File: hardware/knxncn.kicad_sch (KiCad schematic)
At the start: 23 parts, among them U1 NCN5130, X1 FA-238

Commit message: Switch to STM32U575CIT6
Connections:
- net GND: now also U1.23 (MODE1), U1.24 (MODE2), U1.25 (TREQ), U1.26 (CSB/UC1), U1.29 (SCK/UC2)
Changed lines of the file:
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@@
   (junction (at 186.69 85.09) (diameter 0) (color 0 0 0 0)
   )
+  (junction (at 179.07 72.39) (diameter 0) (color 0 0 0 0)
+  )
   (junction (at 96.52 77.47) (diameter 0) (color 0 0 0 0)
   )
@@
   )
   (junction (at 124.46 110.49) (diameter 0) (color 0 0 0 0)
+  )
+  (junction (at 179.07 69.85) (diameter 0) (color 0 0 0 0)
   )
   (junction (at 161.29 110.49) (diameter 0) (color 0 0 0 0)
@@
     (stroke (width 0) (type default) (color 0 0 0 0))
   )
+  (wire (pts (xy 179.07 69.85) (xy 179.07 72.39))
+    (stroke (width 0) (type default) (color 0 0 0 0))
+  )
   (wire (pts (xy 105.41 87.63) (xy 105.41 85.09))
     (stroke (width 0) (type default) (color 0 0 0 0))
@@
     (stroke (width 0) (type default) (color 0 0 0 0))
   )
-  (wire (pts (xy 165.1 72.39) (xy 186.69 72.39))
+  (wire (pts (xy 165.1 72.39) (xy 179.07 72.39))
     (stroke (width 0) (type default) (color 0 0 0 0))
   )
@@
     (stroke (width 0) (type default) (color 0 0 0 0))
   )
+  (wire (pts (xy 179.07 72.39) (xy 186.69 72.39))
+    (stroke (width 0) (type default) (color 0 0 0 0))
+  )

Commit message: Progress
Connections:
- net GND is gone; now on net GNDREF: C6.2, U1.23 (MODE1), U1.24 (MODE2), U1.25 (TREQ), U1.26 (CSB/UC1), U1.29 (SCK/UC2), U1.31 (VSSD), U1.33 (XSEL), U1.41 (GND)
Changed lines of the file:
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@@
   (junction (at 77.47 92.71) (diameter 0) (color 0 0 0 0)
+  )
+  (junction (at 186.69 87.63) (diameter 0) (color 0 0 0 0)
   )
   (junction (at 168.91 69.85) (diameter 0) (color 0 0 0 0)
@@
     (effects (font (size 1.27 1.27)) (justify left bottom))
   )
-  (label "KNX-" (at 77.47 102.87 180)
-    (effects (font (size 1.27 1.27)) (justify right bottom))
-  )
-  (hierarchical_label "KNX_GND" (shape output) (at 176.53 133.35 0)
+  (hierarchical_label "GNDREF" (shape output) (at 176.53 133.35 0)
     (effects (font (size 1.27 1.27)) (justify left))
   )
@@
     (effects (font (size 1.27 1.27)) (justify right))
   )
-  (hierarchical_label "KNX_V12" (shape output) (at 111.76 106.68 180)
+  (hierarchical_label "+12V" (shape output) (at 111.76 106.68 180)
     (effects (font (size 1.27 1.27)) (justify right))
   )
@@
     (effects (font (size 1.27 1.27)) (justify left))
   )
-  (hierarchical_label "KNX_V3.3" (shape output) (at 173.99 104.14 0)
+  (hierarchical_label "+3.3V" (shape output) (at 173.99 104.14 0)
     (effects (font (size 1.27 1.27)) (justify left))
   )
@@
     (pin "2")
   )
-  (symbol (lib_id "power:GND") (at 153.67 52.07 180) (unit 1)
-    (in_bom yes) (on_board yes)
-    (property "Reference" "#PWR0130" (id 0) (at 153.67 45.72 0)
-      (effects (font (size 1.27 1.27)) hide)
-    )
-    (property "Value" "GND" (id 1) (at 153.543 47.6758 0))
-    (property "Footprint" "" (id 2) (at 153.67 52.07 0)
-      (effects (font (size 1.27 1.27)) hide)
-    )
-    (property "Datasheet" "" (id 3) (at 153.67 52.07 0)
-      (effects (font (size 1.27 1.27)) hide)
-    )
-    (pin "1")
-  )
   (symbol (lib_id "KnxBoard-rescue:+3.3V-power") (at 173.99 110.49 270) (unit 1)
     (in_bom yes) (on_board yes)
@@
     (pin "1")
     (pin "2")
-  )
-  (symbol (lib_id "power:GND") (at 179.07 69.85 90) (unit 1)
-    (in_bom yes) (on_board yes)
-    (property "Reference" "#PWR0131" (id 0) (at 185.42 69.85 0)
-      (effects (font (size 1.27 1.27)) hide)
-    )
-    (property "Value" "GND" (id 1) (at 183.4642 69.723 0))
-    (property "Footprint" "" (id 2) (at 179.07 69.85 0)
-      (effects (font (size 1.27 1.27)) hide)
-    )
-    (property "Datasheet" "" (id 3) (at 179.07 69.85 0)
-      (effects (font (size 1.27 1.27)) hide)
-    )
-    (pin "1")
   )
   (symbol (lib_id "Device:C") (at 116.84 121.92 0) (unit 1)
@@
     (pin "1")
   )
+  (symbol (lib_id "power:GNDREF") (at 186.69 87.63 0) (unit 1)
+    (in_bom yes) (on_board yes)
+    (property "Reference" "#PWR0133" (id 0) (at 186.69 93.98 0)
+      (effects (font (size 1.27 1.27)) hide)
+    )
+    (property "Value" "GNDREF" (id 1) (at 193.04 90.17 0))
+    (property "Footprint" "" (id 2) (at 186.69 87.63 0)
+      (effects (font (size 1.27 1.27)) hide)
+    )
+    (property "Datasheet" "" (id 3) (at 186.69 87.63 0)
+      (effects (font (size 1.27 1.27)) hide)
+    )
+    (pin "1")
+  )
+  (symbol (lib_id "power:GNDREF") (at 179.07 69.85 90) (unit 1)
+    (in_bom yes) (on_board yes)
+    (property "Reference" "#PWR0124" (id 0) (at 185.42 69.85 0)
+      (effects (font (size 1.27 1.27)) hide)
+    )
+    (property "Value" "GNDREF" (id 1) (at 181.61 63.5 0))
+    (property "Footprint" "" (id 2) (at 179.07 69.85 0)
+      (effects (font (size 1.27 1.27)) hide)
+    )
+    (property "Datasheet" "" (id 3) (at 179.07 69.85 0)
+      (effects (font (size 1.27 1.27)) hide)
+    )
+    (pin "1")
+  )
   (symbol (lib_id "Device:C") (at 161.29 121.92 0) (unit 1)
     (in_bom yes) (on_board yes)
@@
     (pin "2")
   )
-  (symbol (lib_id "power:GND") (at 120.65 97.79 0) (unit 1)
-    (in_bom yes) (on_board yes)
-    (property "Reference" "#PWR0124" (id 0) (at 120.65 104.14 0)
-      (effects (font (size 1.27 1.27)) hide)
-    )
-    (property "Value" "GND" (id 1) (at 120.777 102.1842 0))
-    (property "Footprint" "" (id 2) (at 120.65 97.79 0)
-      (effects (font (size 1.27 1.27)) hide)
-    )
-    (property "Datasheet" "" (id 3) (at 120.65 97.79 0)
-      (effects (font (size 1.27 1.27)) hide)
-    )
-    (pin "1")
-  )
   (symbol (lib_id "Device:R") (at 135.89 116.84 180) (unit 1)
     (in_bom yes) (on_board yes)
@@
     (pin "1")
     (pin "2")
+  )
+  (symbol (lib_id "power:GNDREF") (at 153.67 52.07 180) (unit 1)
+    (in_bom yes) (on_board yes)
+    (property "Reference" "#PWR?" (id 0) (at 153.67 45.72 0)
+      (effects (font (size 1.27 1.27)) hide)
+    )
+    (property "Value" "GNDREF" (id 1) (at 147.32 49.53 0))
+    (property "Footprint" "" (id 2) (at 153.67 52.07 0)
+      (effects (font (size 1.27 1.27)) hide)
+    )
+    (property "Datasheet" "" (id 3) (at 153.67 52.07 0)
+      (effects (font (size 1.27 1.27)) hide)
+    )
+    (pin "1")
   )
   (symbol (lib_id "power:GNDREF") (at 91.44 102.87 0) (unit 1)
@@
       (effects (font (size 1.27 1.27)) hide)
     )
+    (pin "1")
+  )
+  (symbol (lib_id "power:GNDREF") (at 120.65 97.79 0) (unit 1)
+    (in_bom yes) (on_board yes)
+    (property "Reference" "#PWR0131" (id 0) (at 120.65 104.14 0)
+      (effects (font (size 1.27 1.27)) hide)
+    )
+    (property "Value" "GNDREF" (id 1) (at 127 100.33 0))
+    (property "Footprint" "" (id 2) (at 120.65 97.79 0)
+      (effects (font (size 1.27 1.27)) hide)
+    )
+    (property "Datasheet" "" (id 3) (at 120.65 97.79 0)
+      (effects (font (size 1.27 1.27)) hide)
+    )

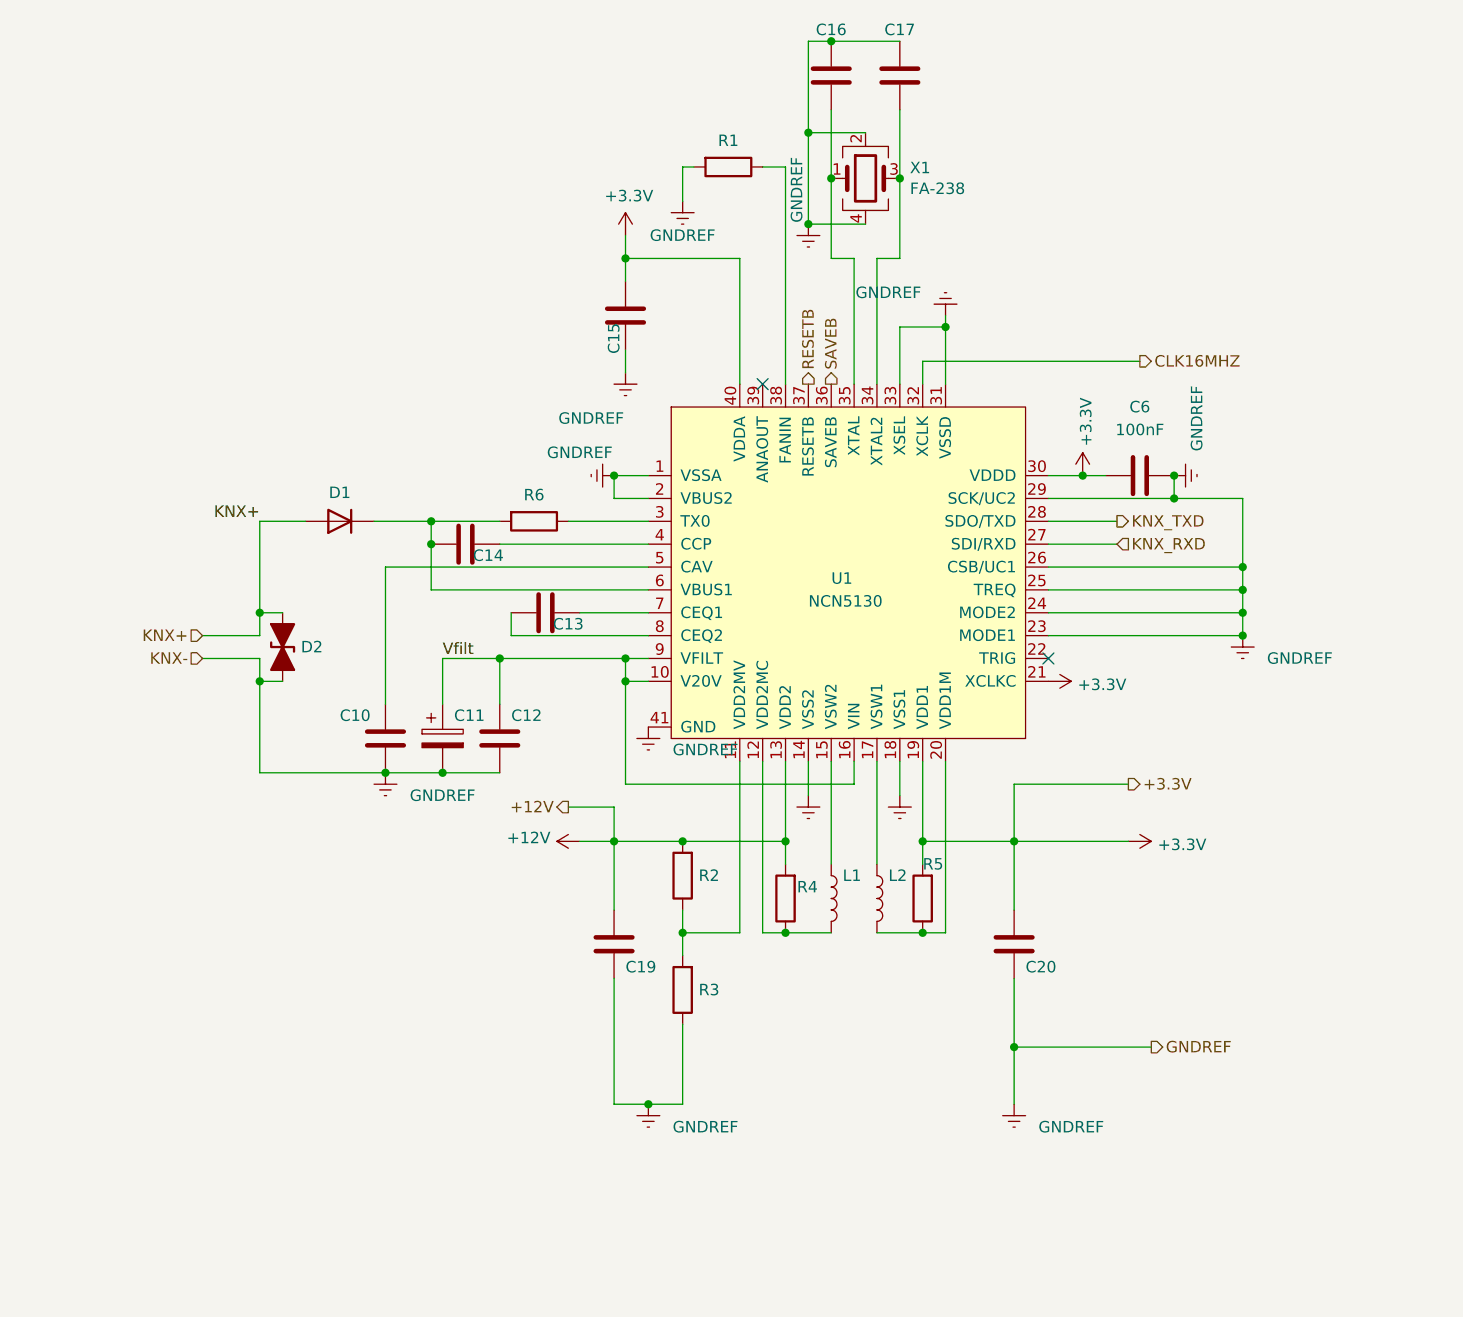
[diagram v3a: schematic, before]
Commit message: Add 3D model and remove old parts
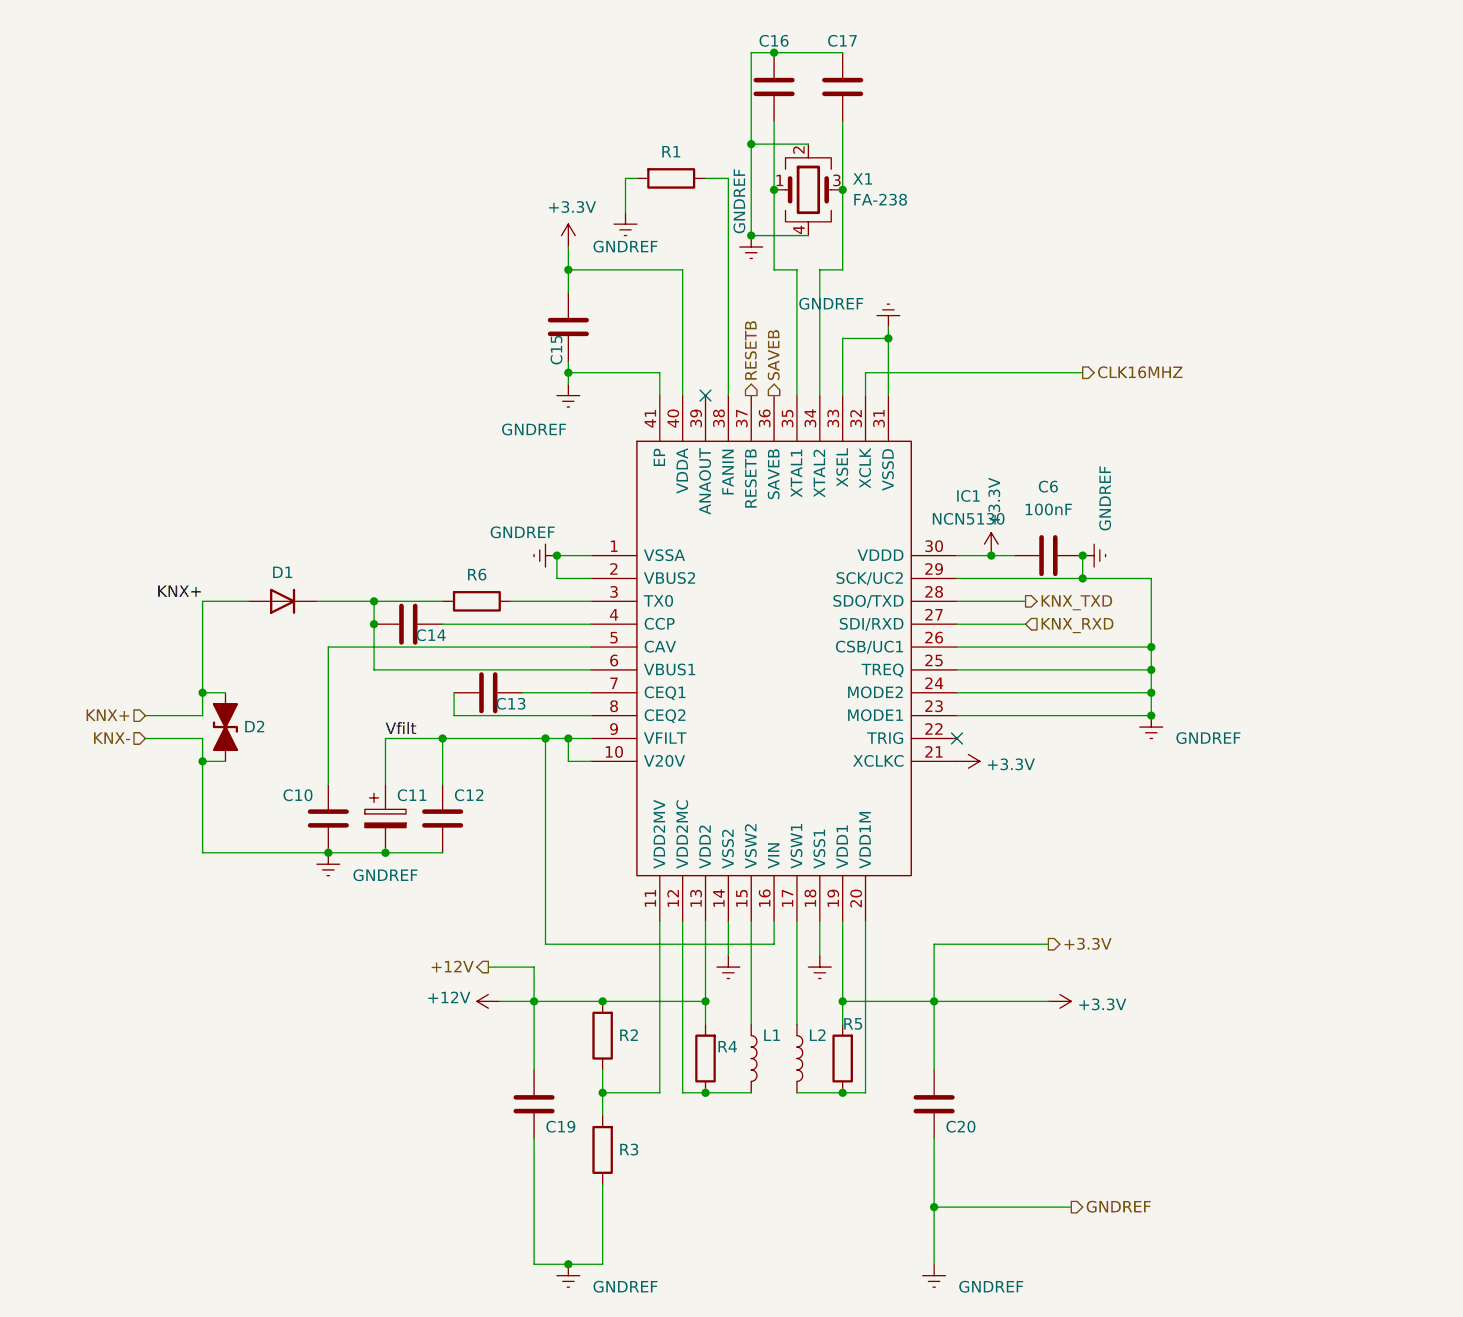
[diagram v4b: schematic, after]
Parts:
- removed U1: NCN5130, Package_DFN_QFN:QFN-40-1EP_6x6mm_P0.5mm_EP4.6x4.6mm_ThermalVias, symbol KNX_NCN5130:NCN5130
- added IC1: NCN5130, KnxBoard:NCN5130, symbol NCN5130:NCN5130
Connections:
- net +12V: now also IC1.13 (VDD2)
- net +3V3: now also IC1.19 (VDD1), IC1.21 (XCLKC), IC1.30 (VDDD), IC1.40 (VDDA)
- net CLK16MHZ: now also IC1.32 (XCLK)
- net GNDREF: now also IC1.1 (VSSA), IC1.14 (VSS2), IC1.18 (VSS1), IC1.2 (VBUS2), IC1.23 (MODE1), IC1.24 (MODE2), IC1.25 (TREQ), IC1.26 (CSB/UC1), IC1.29 (SCK/UC2), IC1.31 (VSSD), IC1.33 (XSEL), IC1.41 (EP)
- net KNX_RXD: now also IC1.27 (SDI/RXD)
- net KNX_TXD: now also IC1.28 (SDO/TXD)
- net RESETB: now also IC1.37 (RESETB)
- net SAVEB: now also IC1.36 (SAVEB)
- net Vfilt: now also IC1.10 (V20V), IC1.16 (VIN), IC1.9 (VFILT)
- net at R1.1: now also IC1.38 (FANIN)
- net at C14.1: now also IC1.4 (CCP)
- net at C14.2, D1.1 (K), R6.2: now also IC1.6 (VBUS1)
- net at C16.2, X1.1: now also IC1.35 (XTAL1)
- net at C17.2, X1.3: now also IC1.34 (XTAL2)
- net at C10.1: now also IC1.5 (CAV)
- net at L1.2, R4.1: now also IC1.12 (VDD2MC)
- net at L2.2, R5.1: now also IC1.20 (VDD1M)
- net at R2.1, R3.2: now also IC1.11 (VDD2MV)
- net at L2.1: now also IC1.17 (VSW1)
- net at L1.1: now also IC1.15 (VSW2)
- net at R6.1: now also IC1.3 (TX0)
- net at C13.1: now also IC1.7 (CEQ1)
- net at C13.2: now also IC1.8 (CEQ2)
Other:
- moved on the sheet: C10, C11, C12, C13, C14, C15, C16, C17, C19, C20, C6, D1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

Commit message: Routage OK need check and mass and texts
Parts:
- removed C11: 100uF 35V, Capacitor_SMD:CP_Elec_6.3x7.7, symbol KnxBoard-rescue:CP-Device
- removed D2: 1SMA40CA, Diode_SMD:D_SMA, symbol KnxBoard-rescue:D_TVS_ALT-Device
- added C8: 100nF 50V, Capacitor_SMD:C_0603_1608Metric_Pad1.08x0.95mm_HandSolder, symbol Device:C
- added C9: 100uF 35V, Capacitor_SMD:CP_Elec_6.3x7.7, symbol Device:C_Polarized
- added D2: 1SMA40CA, Diode_SMD:D_SMA, symbol Device:D_TVS
- added J4: Conn_01x02, KnxBoard:KNX_Connector, symbol Connector_Generic:Conn_01x02
- added JP1: Clock_8_16, Jumper:SolderJumper-3_P1.3mm_Open_RoundedPad1.0x1.5mm, symbol Jumper:SolderJumper_3_Bridged12
- added JP2: Parity, Jumper:SolderJumper-3_P1.3mm_Open_RoundedPad1.0x1.5mm, symbol Jumper:SolderJumper_3_Bridged12
- added JP3: Speed, Jumper:SolderJumper-3_P1.3mm_Open_RoundedPad1.0x1.5mm, symbol Jumper:SolderJumper_3_Bridged12
- C10: renamed from C12; value 1uF 35V ESR < 2ohm -> 1uF 50V ESR < 2ohm
- D1: value SS16 -> SS16T3G
- renumbered C19 to C11, C20 to C12, C15 to C3, C6 to C4, C14 to C5, C13 to C6, C10 to C7, L1 to L2, L2 to L3, R6 to R10, R2 to R18, R4 to R20, R5 to R21, R3 to R22, R1 to R3
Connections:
- net +3V3: now also JP1.3 (B), JP2.3 (B), JP3.3 (B)
- net GNDREF: now also C8.2, C9.2, D2.1 (A1), J4.1 (Pin_1), JP1.1 (A), JP2.1 (A), JP3.1 (A); no longer IC1.26 (CSB/UC1), IC1.29 (SCK/UC2), IC1.33 (XSEL)
- net KNX+: now also D2.2 (A2), J4.2 (Pin_2)
- net Vfilt: now also C8.1, C9.1; no longer C10.1, IC1.10 (V20V)
- new net: IC1.33 (XSEL), JP1.2 (C)
- new net: IC1.26 (CSB/UC1), JP3.2 (C)
- new net: C10.1, IC1.10 (V20V)
- new net: IC1.29 (SCK/UC2), JP2.2 (C)
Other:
- moved on the sheet: C7
